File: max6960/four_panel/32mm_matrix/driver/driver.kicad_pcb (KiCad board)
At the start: 2 copper layers, 64 x 64 mm, 20 parts, among them M1 LED-MATRIX-8X8, M2 LED-MATRIX-8X8, M3 LED-MATRIX-8X8, M4 LED-MATRIX-8X8, P1 CONN_2X2, U1 MAX6960, U2 74AHC1G126, U3 MAX6960, U4 CONN15, U5 CONN15

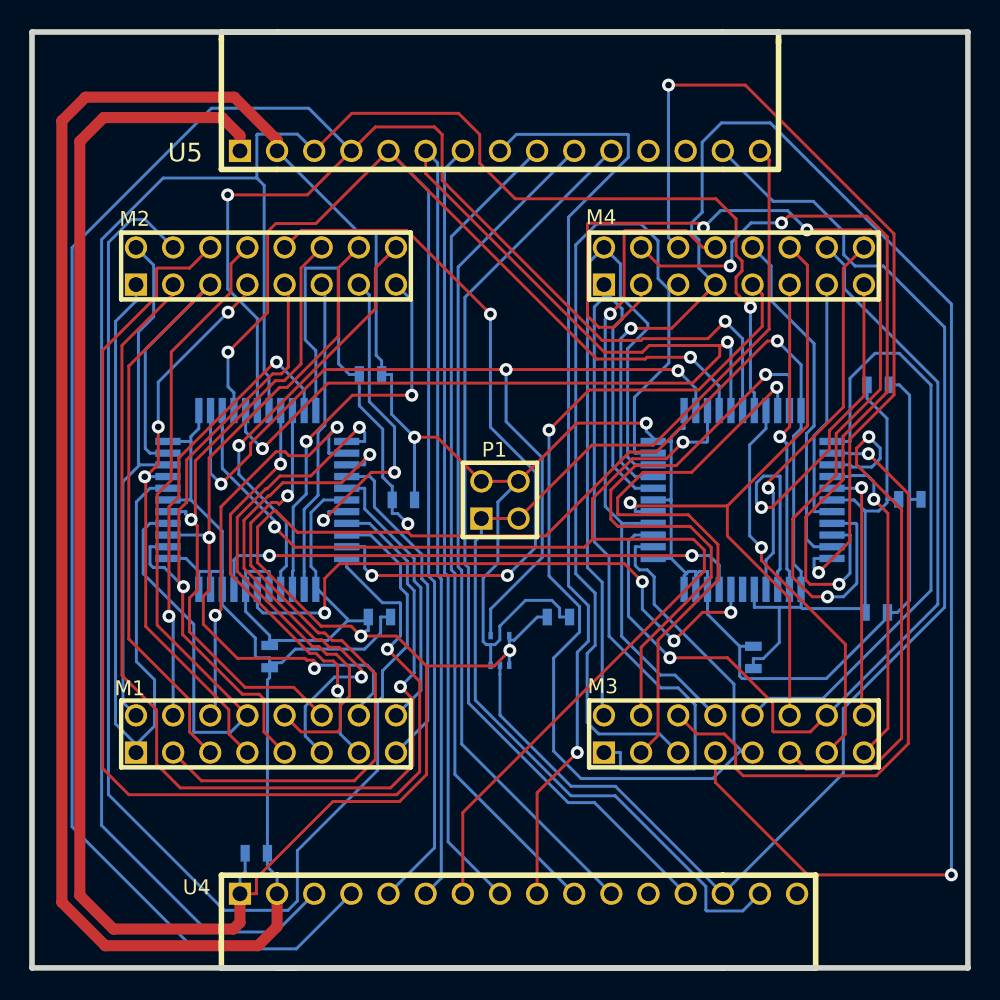
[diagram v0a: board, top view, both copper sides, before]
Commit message: Fixed errors in four panel 32mm matrix driver.
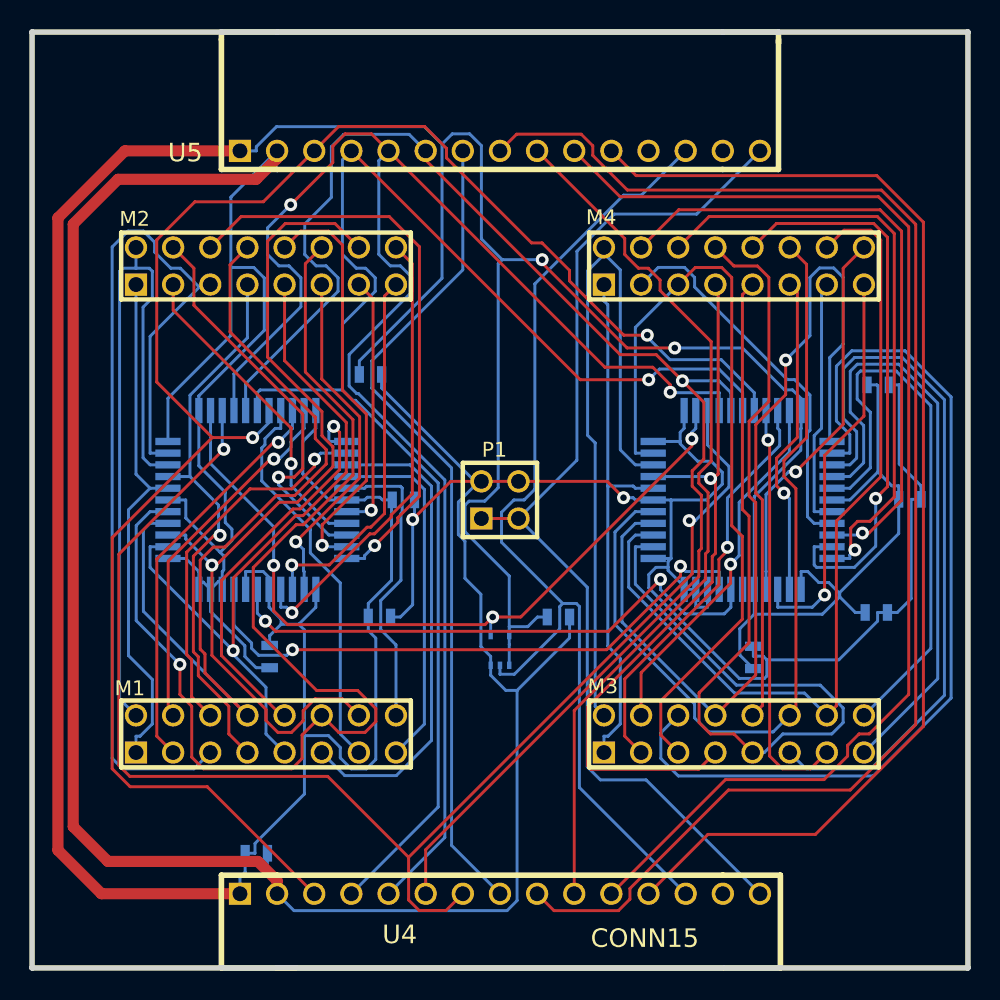
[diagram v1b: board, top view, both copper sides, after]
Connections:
- U3 pad 39: (no net) -> N-000001
- U4 pad 12: (no net) -> /CS6
- U4 pad 13: /CS6 -> /OSC
- U4 pad 14: /OSC -> N-0000035
- U5 pad 12: (no net) -> N-0000066
- U5 pad 13: (no net) -> /OSC
- U5 pad 14: /OSC -> N-0000036
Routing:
- net /COL_A11: track 90.9 -> 27.3 mm, vias 0 -> 1
- net /ROW_B6: track 112.3 -> 50.3 mm, vias 2 -> 1
- net /CLK: track 154.5 -> 101.1 mm, vias 2 -> 1
- net /COL_A10: track 74.2 -> 22.0 mm
- net /COL_B10: track 70.2 -> 26.3 mm, vias 3 -> 0
- net /COL_A13: track 81.1 -> 40.1 mm
- net /ROW_A4: track 44.1 -> 78.6 mm
- net /CS3: track 64.9 -> 98.1 mm, vias 1 -> 0
- net GND: track 276.5 -> 308.9 mm
- net /RST: track 142.7 -> 116.8 mm, vias 1 -> 2
- net /CS5: track 58.4 -> 83.4 mm
- net /ROW_B5: track 60.2 -> 36.3 mm
- net /COL_B8: track 17.7 -> 39.2 mm, vias 1 -> 0
- net /COL_B5: track 42.7 -> 63.7 mm, vias 1 -> 0
- net /COL_A12: track 49.5 -> 29.0 mm, vias 3 -> 1
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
